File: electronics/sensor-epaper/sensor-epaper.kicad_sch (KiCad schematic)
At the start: 52 parts, among them J1 i2c, J2 SWD, J4 Display, Q1 Q_NMOS_GSD, U2 ATSAMD21G18A-A, Y1 32.768

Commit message: Implement fixes for v1.0.0 board: * Fixed mirrored display connector * Fixed wrong button pinout * Remove CS from GPIO11 which is VDD_SPI after all, add a requisite cap * Add tantallum bulk cap, add more capacitance near MCU to counter power gulp related resets using thin USB cable * Consolidate some passive values
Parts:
- removed C1, C2: 22p, Capacitor_SMD:C_0402_1005Metric, symbol Device:C
- removed C19, C20, C3, C4, C5, C6: 1u, Capacitor_SMD:C_0402_1005Metric, symbol Device:C
- removed J2: SWD, miceuz-lib:TC2030-MCP-NL, symbol Connector:Conn_01x06_Female
- removed R1, R2: 1k, Resistor_SMD:R_0603_1608Metric, symbol Device:R
- removed R19: 1M, Resistor_SMD:R_0603_1608Metric, symbol Device:R
- removed TP1, TP2, TP3, TP4, TP5: TestPoint, TestPoint:TestPoint_Pad_D1.5mm, symbol Connector:TestPoint
- removed U2: ATSAMD21G18A-A, Package_QFP:TQFP-48_7x7mm_P0.5mm, symbol MCU_Microchip_SAMD:ATSAMD21G18A-A
- removed Y1: 32.768, Crystal:Crystal_SMD_3215-2Pin_3.2x1.5mm, symbol Device:Crystal
- added AE1: PCB Antenna, miceuz-lib:Texas_SWRA117D_2.4GHz_Left, symbol Device:Antenna
- added C1: 100u, Capacitor_Tantalum_SMD:CP_EIA-3528-15_AVX-H, symbol Device:C_Polarized
- added C21, C25, C34, C46: 22u, Capacitor_SMD:C_0603_1608Metric, symbol Device:C
- added C22, C24, C26, C28, C29, C32, C33, C35, C40, C41, C47: 1u, Capacitor_SMD:C_0402_1005Metric, symbol Device:C
- added C30, C31: 18p, Capacitor_SMD:C_0402_1005Metric, symbol Device:C
- added C36, C37: ?, Capacitor_SMD:C_0402_1005Metric, symbol Device:C
- added C38, C39: 12p, Capacitor_SMD:C_0402_1005Metric, symbol Device:C
- added C42: 10p, Capacitor_SMD:C_0402_1005Metric, symbol Device:C
- added C43, C44: 4u7, Capacitor_SMD:C_0402_1005Metric, symbol Device:C
- added D1: 1N4148, Diode_SMD:D_SOD-123, symbol Device:D
- added J2: Conn_01x06, Connector_PinHeader_2.54mm:PinHeader_1x05_P2.54mm_Vertical, symbol Connector_Generic:Conn_01x05
- added J3: Ufl, Connector_Coaxial:U.FL_Hirose_U.FL-R-SMT-1_Vertical, symbol Connector:Conn_Coaxial
- added J9: USB micro, miceuz-lib:XKB_U254-051T-4BH83-F1S, symbol Connector:USB_B_Micro
- added L2: 10u 1A, Inductor_SMD:L_Taiyo-Yuden_NR-60xx, symbol Device:L
- added L3: 0, Inductor_SMD:L_0402_1005Metric, symbol Device:L
- added Q3: NX2301P, Package_TO_SOT_SMD:SOT-23, symbol Device:Q_PMOS_GSD
- added R12, R13, R21, R22: 1M, Resistor_SMD:R_0603_1608Metric, symbol Device:R
- added R14: 0, Resistor_SMD:R_0402_1005Metric, symbol Device:R
- added R15: 300k, Resistor_SMD:R_0603_1608Metric, symbol Device:R
- added R16: 348k, Resistor_SMD:R_0603_1608Metric, symbol Device:R
- added R17: 200k, Resistor_SMD:R_0603_1608Metric, symbol Device:R
- added R23, R4: 4.7k, Resistor_SMD:R_0603_1608Metric, symbol Device:R
- added R24: 150, Resistor_SMD:R_0603_1608Metric, symbol Device:R
- added R3: ?, Resistor_SMD:R_0402_1005Metric, symbol Device:R
- added SW1: SW_Push, miceuz-lib:SHOUHAN_TS24CA, symbol Switch:SW_Push
- added U1: ESP32-C3FN4, Package_DFN_QFN:QFN-32-1EP_5x5mm_P0.5mm_EP3.7x3.7mm_ThermalVias, symbol miceuz:ESP32-C3FN4
- added U2: AMS1117-3.3, Package_TO_SOT_SMD:SOT-223-3_TabPin2, symbol Regulator_Linear:AMS1117-3.3
- added U3: NCP1421, Package_SO:MSOP-8_3x3mm_P0.65mm, symbol Regulator_Switching:AP3012
- added Y2: 32kHz, Crystal:Crystal_SMD_2012-2Pin_2.0x1.2mm, symbol Device:Crystal_Small
- added Y3: 40MHz 10ppm, Crystal:Crystal_SMD_2016-4Pin_2.0x1.6mm, symbol Device:Crystal_GND24_Small
- BT1, BT2: footprint miceuz-lib:2450_battery -> miceuz-lib:AA_KEYCO_53_SMD; Manufacturer (none) -> KEYSTONE; PartNo (none) -> 53
- C10, C11, C13, C14, C16, C17, C18, C23, C27, C7, C8, C9: LCSC (none) -> C52923
- C12, C15: LCSC (none) -> C19666
- D3, D4, D5: LCSC (none) -> C8598
- FID1, FID2: DNF (none) -> DNF; now not fitted
- J1: DNF (none) -> DNF; now not fitted; now left out of the parts list
- J4: LCSC (none) -> C262643
- L1: LCSC (none) -> C38117; Manufacturer Taiyo Yuden -> Sunlord; PartNo NRS4018T100MDGJ -> SWPA4030S100MT
- Q1: LCSC (none) -> C699302
- R11, R20: value 1k -> 4.7k; LCSC (none) -> C23162
- R18: value 1M -> 220k; LCSC (none) -> C22961
- R5: value 10k -> 4.7k; LCSC (none) -> C23162
- R6: LCSC (none) -> C103895
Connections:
- net +BATT: now also Q3.3 (D); no longer BT1.1 (+), C12.1, C8.1, J4.15 (Pin_15), J4.16 (Pin_16), L1.1, R11.1, R18.1
- net BATT_VOLTAGE: now also C24.1, R12.2, R13.1, U1.8 (GPIO3/ADC1_CH3); no longer C27.1, R18.2
- net D+: now also J9.3 (D+), U1.26 (USB_D­P/GPIO19)
- net D-: now also J9.2 (D-), U1.25 (USB_D­N/GPIO18)
- net DISPLAY_BUSY: now also U1.16 (GPIO10)
- net D/C: now also J2.1 (Pin_1), R22.1, U1.15 (GPIO9)
- net GND: now also C1.2, C21.2, C22.2, C24.2, C25.2, C26.2, C28.2, C29.2, C30.2, C31.2, C32.2, C33.2, C34.2, C35.2, C36.2, C37.2, C38.2, C39.2, C40.2, C41.2, C43.2, C44.2, C46.2, C47.2, J2.5 (Pin_5), J3.2 (Ext), J9.5 (GND), J9.6 (Shield), R13.2, R15.2, R17.2, R23.2, SW1.1, U1.33 (GND), U2.1 (GND), U3.6 (GND), Y3.2, Y3.4; no longer BT2.2 (-)
- net I2C_SCL: now also U1.10 (MTDI/GPIO5/ADC2_CH0/FSPIWP)
- net I2C_SDA: now also U1.9 (MTMS/GPIO4/ADC1_CH4/FSPIHD)
- net SPI_CLK: now also U1.12 (MTCK/GPIO6/FSPICLK)
- net SPI_DATA: now also U1.13 (MTDO/GPIO7/FSPID)
- net TXD: now also R20.2, R24.1, U1.28 (U0TXD/GPIO21)
- net ~{CS}: now also J2.2 (Pin_2), U1.27 (U0RXD/GPIO20)
- net ~{DISPLAY_RESET}: now also U1.14 (GPIO8)
- net ~{I2C_ENABLE}: now also R21.2, U1.6 (GPIO2/ADC1_CH2/FSPIQ)
- net SW_NODE_DISPLAY: now reaches C15.2, D5.2 (A), L1.2, Q1.3 (D)
- net I2C-interface/VOUT renamed VI2C
- new net: C47.1, U1.18 (VDD_SPI/GPIO11)
- new net: J2.3 (Pin_3), R24.2
- new net +3V3: C1.1, C12.1, C21.1, C22.1, C28.1, C29.1, C32.1, C33.1, C34.1, C40.1, C41.1, C42.1, C46.1, C8.1, J4.15 (Pin_15), J4.16 (Pin_16), L1.1, R11.1, R16.1, R21.1, R22.2, R4.1, U1.11 (VDD3P3_RTC), U1.17 (VDD3P3_CPU), U1.2 (VDD3P3), U1.3 (VDD3P3), U1.31 (VDDA), U1.32 (VDDA), U3.8 (OUT)
- new net ANT: C36.1, J3.1 (In), L3.1, U1.1 (LNA_IN)
- new net ANT_COMP: AE1.1 (A), C37.1, L3.2
- new net CHIP_EN: C35.1, J2.4 (Pin_4), R4.2, SW1.2, U1.7 (CHIP_EN)
- new net EN_MAIN: R15.1, R18.2, U3.2 (EN)
- new net FB_MAIN: C42.2, R16.2, R17.1, U3.1 (FB)
- new net MID_BATT: BT1.1 (+), BT2.2 (-)
- new net REF_MAIN: C27.1, U3.4 (REF)
- new net SW_MAIN: L2.2, U3.7 (LX)
- new net USB_3V3: C44.1, D1.2 (A), U2.2 (VO)
- new net VBUS: C43.1, J9.1 (VBUS), Q3.1 (G), R23.1, U2.3 (VI)
- new net VIN: C25.1, C26.1, D1.1 (K), L2.1, Q3.2 (S), R12.1, R18.1, U3.5 (BAT)
- new net XTAL_32K_N: C30.1, R3.2, U1.5 (GPIO1/ADC1_CH1/XTAL_32K_N), Y2.1
- new net XTAL_32K_P: C31.1, R3.1, U1.4 (GPIO0/ADC1_CH0/XTAL_32K_P), Y2.2
- new net XTAL_N: C38.1, U1.29 (XTAL_N), Y3.3
- new net XTAL_P: R14.1, U1.30 (XTAL_P)
- new net XTAL_R_P: C39.1, R14.2, Y3.1
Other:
- note added: "Alternative inductor: NRS4018T100MDGJ by Taiyo Yuden C222882 TYA4012100M-10 by Laird Performance Materials"
- note added: "Alternatives: VLS6045EX-100M NR6045T100M"
- note added: "C30,C31 = 2 * C_{L} - 2 * C_{stray} C_{stray} = 2pF (MCU pin) + 2pF (pcb trace) C30,C31 = 2 * 12.5pF - 2 * 4pF = 17pF"
- note added: "C38,C39 = 2 * C_{L} - 2 * C_{stray} C_{stray} = 2pF (MCU pin) + 2pF (pcb trace) C38,C39 = 2 * 10pF - 2 * 4pF = 12pF"
- note added: "Equivalent series resistance (ESR) <= 70 kΩ."
- note added: "For volume production: Extended Part C347222"
- note added: "TODO: X button pins X consolidate R8, R24 values X decide on VBUS and 3V3 capacitance - electrolytic or not? X consolidate C12 C15 maybe"
- note added: "The parallel resistor R3 is used for biasing the crystal circuit (5 MΩ < R3 < 10 MΩ). In general, you do not need to populate R3."
- note removed: "Alternative inductor: TYA4012100M-10 by Laird Performance Materials"
- note removed: "Tag-Connect TC2030 pinout from datasheet"
- company: (none) -> Catnip electronics
- title: (none) -> Epaper sensor display
- moved on the sheet: BT1, BT2, C10, C11, C12, C13, C14, C15, C16, C17, C18, C23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

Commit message: Add cutout in the PCB to decouple SHT40, fix GND connection
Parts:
- added C48: 1u, Capacitor_SMD:C_0402_1005Metric, symbol Device:C
- added R19, R25: 0, Resistor_SMD:R_0402_1005Metric, symbol Device:R
- added U4: SHT40-AD1B-R2, miceuz-lib:Sensirion_SHT40-AD1B-R2, symbol miceuz:SHT40-AD1B-R2
- C43, C44: value 4u7 -> 1u; LCSC C19666 -> C52923
- J2: footprint Connector_PinHeader_2.54mm:PinHeader_1x05_P2.54mm_Vertical -> Connector_PinHeader_2.54mm:PinHeader_1x07_P2.54mm_Vertical; symbol Connector_Generic:Conn_01x05 -> Connector_Generic:Conn_01x07; now in the parts list
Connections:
- net CHIP_EN: now also J2.6 (Pin_6); no longer J2.4 (Pin_4)
- net GND: now also J2.7 (Pin_7), C48.2, U4.4 (VSS); no longer J2.5 (Pin_5)
- net I2C_SCL: now also U4.2 (SCL)
- net I2C_SDA: now also U4.1 (SDA)
- net VI2C: now also C48.1, U4.3 (VDD)
- net XTAL_32K_N: now also R25.2
- net XTAL_32K_P: now also R19.2
- new net GPIO0: J2.5 (Pin_5), R19.1
- new net GPIO1: J2.4 (Pin_4), R25.1
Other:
- moved on the sheet: J1, SW1

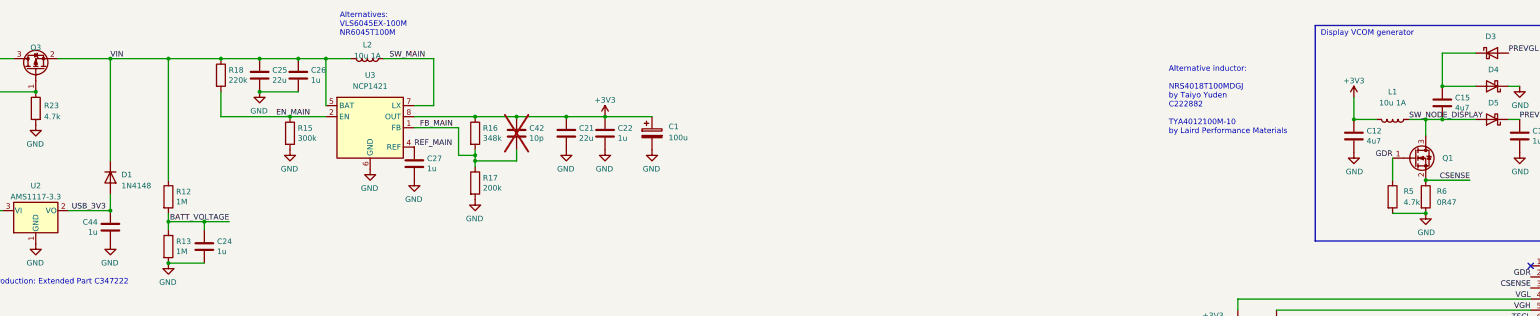
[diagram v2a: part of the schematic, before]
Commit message: Change DC/DC regulator to TPS61023 as previous one is out of stock. Change L1 and R6 to accomodate another display as previous one will be end of life soon
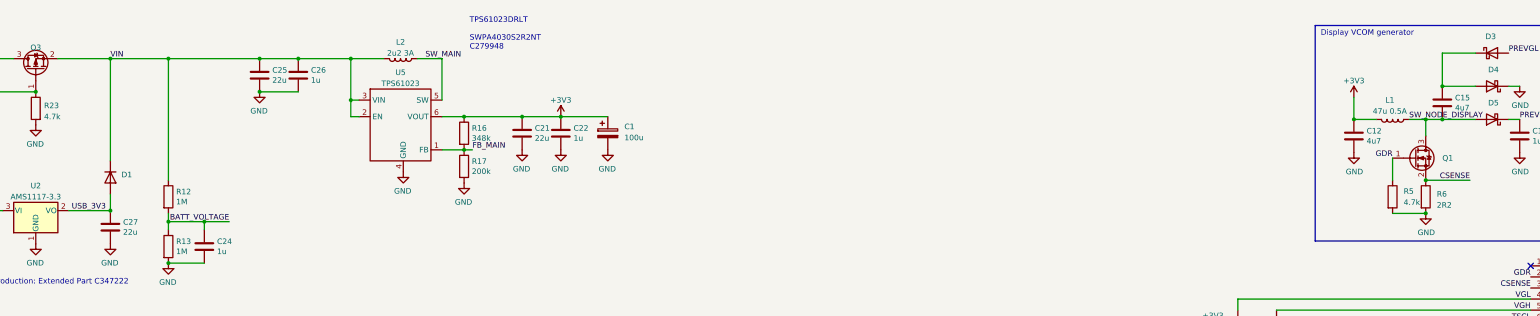
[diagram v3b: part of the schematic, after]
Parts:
- removed C42: 10p, Capacitor_SMD:C_0402_1005Metric, symbol Device:C
- removed C44: 1u, Capacitor_SMD:C_0402_1005Metric, symbol Device:C
- removed R15: 300k, Resistor_SMD:R_0603_1608Metric, symbol Device:R
- removed R18: 220k, Resistor_SMD:R_0603_1608Metric, symbol Device:R
- removed U3: NCP1421, Package_SO:MSOP-8_3x3mm_P0.65mm, symbol Regulator_Switching:AP3012
- added U5: TPS61023, Package_TO_SOT_SMD:SOT-363_SC-70-6_Handsoldering, symbol miceuz:TPS61023
- C27: value 1u -> 22u; footprint Capacitor_SMD:C_0402_1005Metric -> Capacitor_SMD:C_0603_1608Metric; LCSC C52923 -> C60077; PartNo (none) -> CL10A226MP8NUNE
- D1: value 1N4148 -> 2CZ4007; LCSC C81598 -> C85712
- L1: value 10u 1A -> 47u 0.5A; LCSC C38117 -> C354593; Manufacturer Sunlord -> CENKER; PartNo SWPA4030S100MT -> CKCS4030-47uH/M
- L2: value 10u 1A -> 2u2 3A; footprint Inductor_SMD:L_Taiyo-Yuden_NR-60xx -> Inductor_SMD:L_Taiyo-Yuden_NR-40xx; LCSC C79272 -> C279948; Manufacturer Taiyo Yuden -> Sunlord; PartNo NRS4018T100MDGJ -> SWPA4030S2R2NT
- R6: value 0R47 -> 2R2; LCSC C103895 -> C22939
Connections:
- net REF_MAIN is gone; now on net USB_3V3: C27.1
- net +3V3: now also U5.6 (VOUT)
- net FB_MAIN: now also U5.1 (FB)
- net GND: now also U5.4 (GND)
- net SW_MAIN: now also U5.5 (SW)
- net VIN: now also U5.2 (EN), U5.3 (VIN)
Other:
- note added: "TPS61023DRLT SWPA4030S2R2NT C279948"
- note removed: "Alternative inductor: NRS4018T100MDGJ by Taiyo Yuden C222882 TYA4012100M-10 by Laird Performance Materials"
- note removed: "Alternatives: VLS6045EX-100M NR6045T100M"
- title: Epaper sensor display -> Paper WiFi
- moved on the sheet: C1, C21, C22, L2, R16, R17

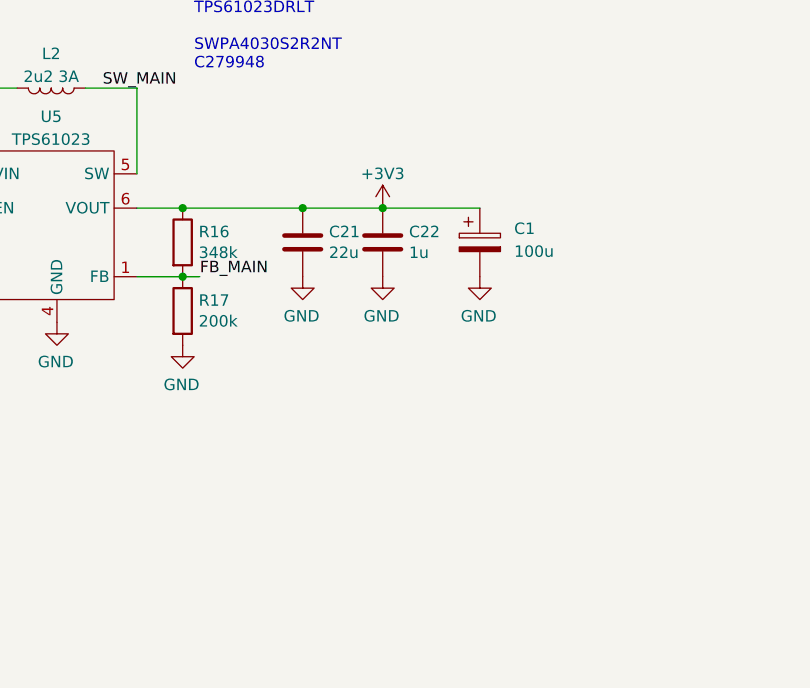
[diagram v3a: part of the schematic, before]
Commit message: Put correct resistor into Dc/Dc converters divider. Fix SC70 footprint
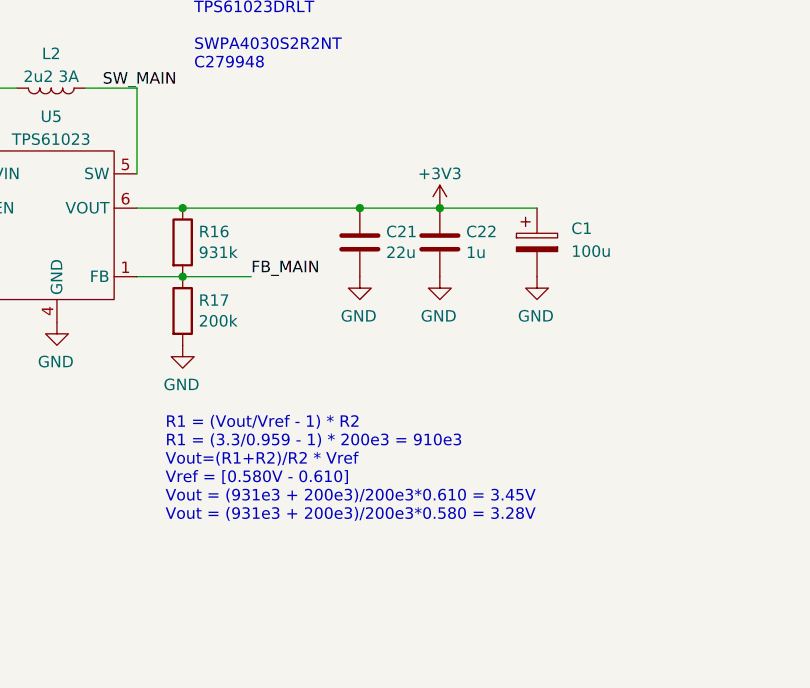
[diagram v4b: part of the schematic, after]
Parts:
- R16: value 348k -> 931k; LCSC C23006 -> C322030
- U5: footprint Package_TO_SOT_SMD:SOT-363_SC-70-6_Handsoldering -> Package_TO_SOT_SMD:SOT-363_SC-70-6
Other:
- note added: "R1 = (Vout/Vref - 1) * R2 R1 = (3.3/0.959 - 1) * 200e3 = 910e3 Vout=(R1+R2)/R2 * Vref Vref = [0.580V - 0.610] Vout = (931e3 + 200e3)/200e3*0.610 = 3.45V Vout = (931e3 + 200e3)/200e3*0.580 = 3.28V"
- moved on the sheet: C1, C21, C22
